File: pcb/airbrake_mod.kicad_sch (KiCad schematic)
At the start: 3 parts

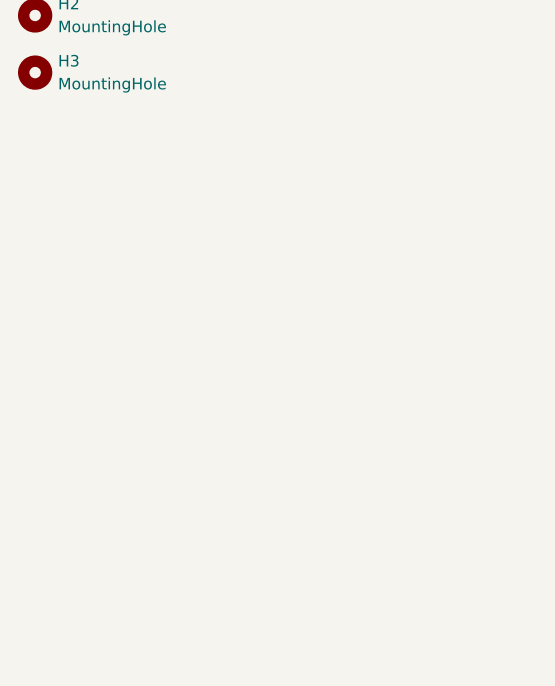
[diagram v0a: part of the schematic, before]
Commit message: Add USB
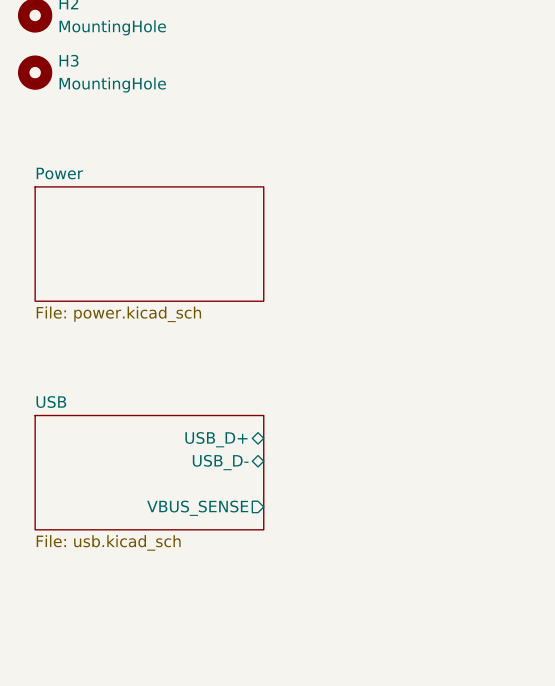
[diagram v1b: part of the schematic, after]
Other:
- added sheet Power (power.kicad_sch)
- added sheet USB (usb.kicad_sch)
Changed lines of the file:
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@@
+		)
+	)
+	(sheet
+		(at 25.4 50.8)
+		(size 25.4 12.7)
+		(exclude_from_sim no)
+		(in_bom yes)
+		(on_board yes)
+		(dnp no)
+		(fields_autoplaced yes)
+		(stroke
+			(width 0.1524)
+			(type solid)
+		)
+		(fill
+			(color 255 255 194 1.0000)
+		)
+		(property "Sheetname" "Power"
+			(at 25.4 50.0884 0)
+			(effects
+				(font
+					(size 1.27 1.27)
+				)
+				(justify left bottom)
+			)
+		)
+		(property "Sheetfile" "power.kicad_sch"
+			(at 25.4 64.0846 0)
+			(effects
+				(font
+					(size 1.27 1.27)
+				)
+				(justify left top)
+			)
+		)
+		(instances
+			(project "airbrake_mod"
+				(path "/1f4fd4ed-9886-4375-a5ac-dc32d5760936"
+					(page "3")
+				)
+			)
+		)
+	)
+	(sheet
+		(at 25.4 76.2)
+		(size 25.4 12.7)
+		(exclude_from_sim no)
+		(in_bom yes)
+		(on_board yes)
+		(dnp no)
+		(fields_autoplaced yes)
+		(stroke
+			(width 0.1524)
+			(type solid)
+		)
+		(fill
+			(color 255 255 194 1.0000)
+		)
+		(property "Sheetname" "USB"
+			(at 25.4 75.4884 0)
+			(effects
+				(font
+					(size 1.27 1.27)
+				)
+				(justify left bottom)
+			)
+		)
+		(property "Sheetfile" "usb.kicad_sch"
+			(at 25.4 89.4846 0)
+			(effects
+				(font
+					(size 1.27 1.27)
+				)
+				(justify left top)
+			)
+		)
+		(pin "USB_D+" bidirectional
+			(at 50.8 78.74 0)
+			(effects
+				(font
+					(size 1.27 1.27)
+				)
+				(justify right)
+			)
+		)
+		(pin "USB_D-" bidirectional
+			(at 50.8 81.28 0)
+			(effects
+				(font
+					(size 1.27 1.27)
+				)
+				(justify right)
+			)
+		)
+		(pin "VBUS_SENSE" output
+			(at 50.8 86.36 0)
+			(effects
+				(font
+					(size 1.27 1.27)
+				)
+				(justify right)
+			)
+		)
+		(instances
+			(project "airbrake_mod"
+				(path "/1f4fd4ed-9886-4375-a5ac-dc32d5760936"
+					(page "4")
+				)
+			)
 		)
 	)

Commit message: Begin power tree design
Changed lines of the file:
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@@
 	)
 	(sheet
-		(at 101.6 76.2)
+		(at 95.25 62.23)
 		(size 25.4 25.4)
 		(exclude_from_sim no)
@@
 		)
 		(property "Sheetname" "MCU"
-			(at 101.6 75.4884 0)
+			(at 95.25 61.5184 0)
 			(effects
 				(font
@@
 		)
 		(property "Sheetfile" "mcu.kicad_sch"
-			(at 101.6 102.1846 0)
+			(at 95.25 88.2146 0)
 			(effects
 				(font

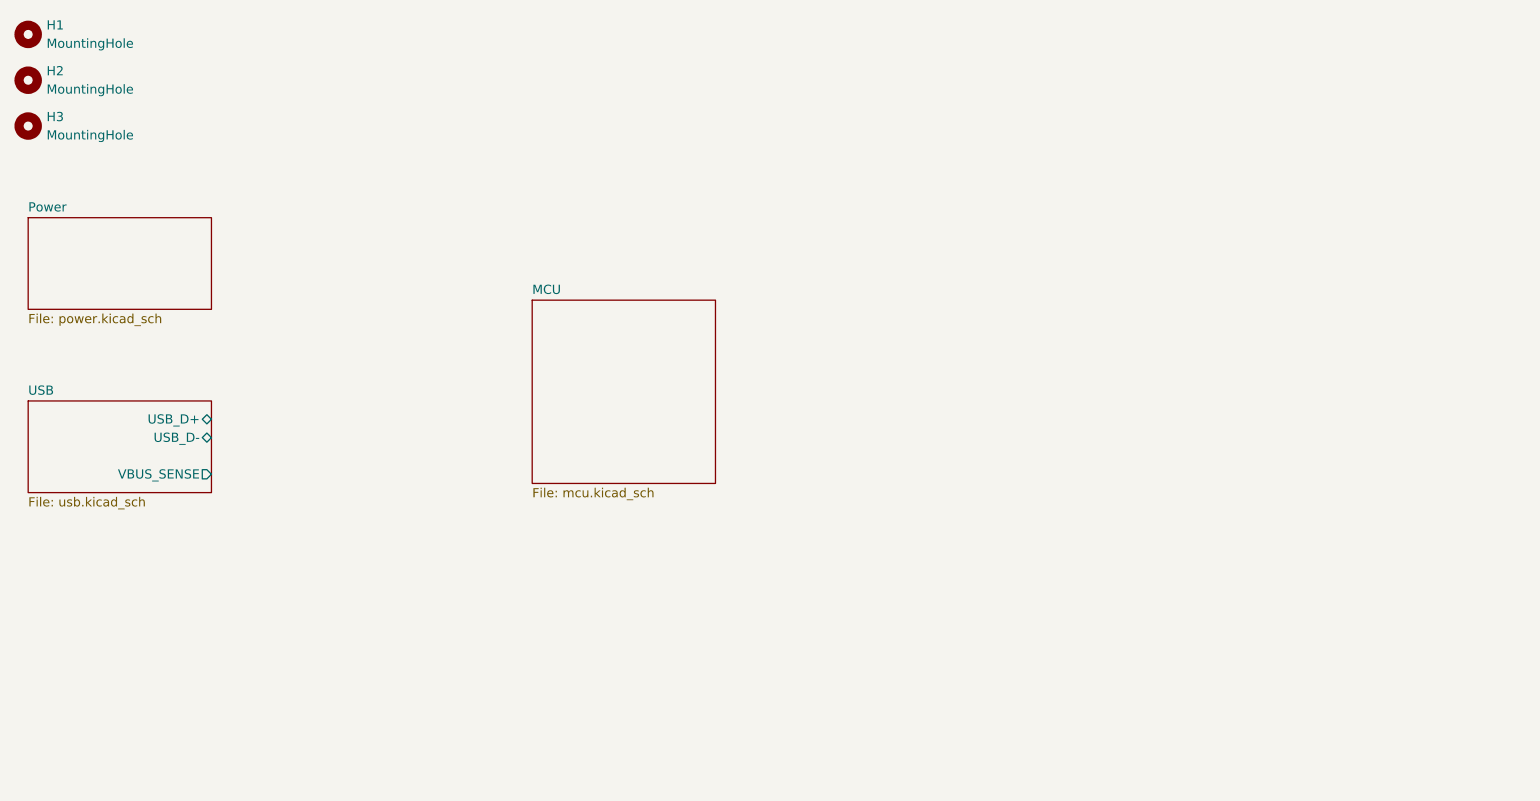
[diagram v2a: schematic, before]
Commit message: Implement flash memory connection
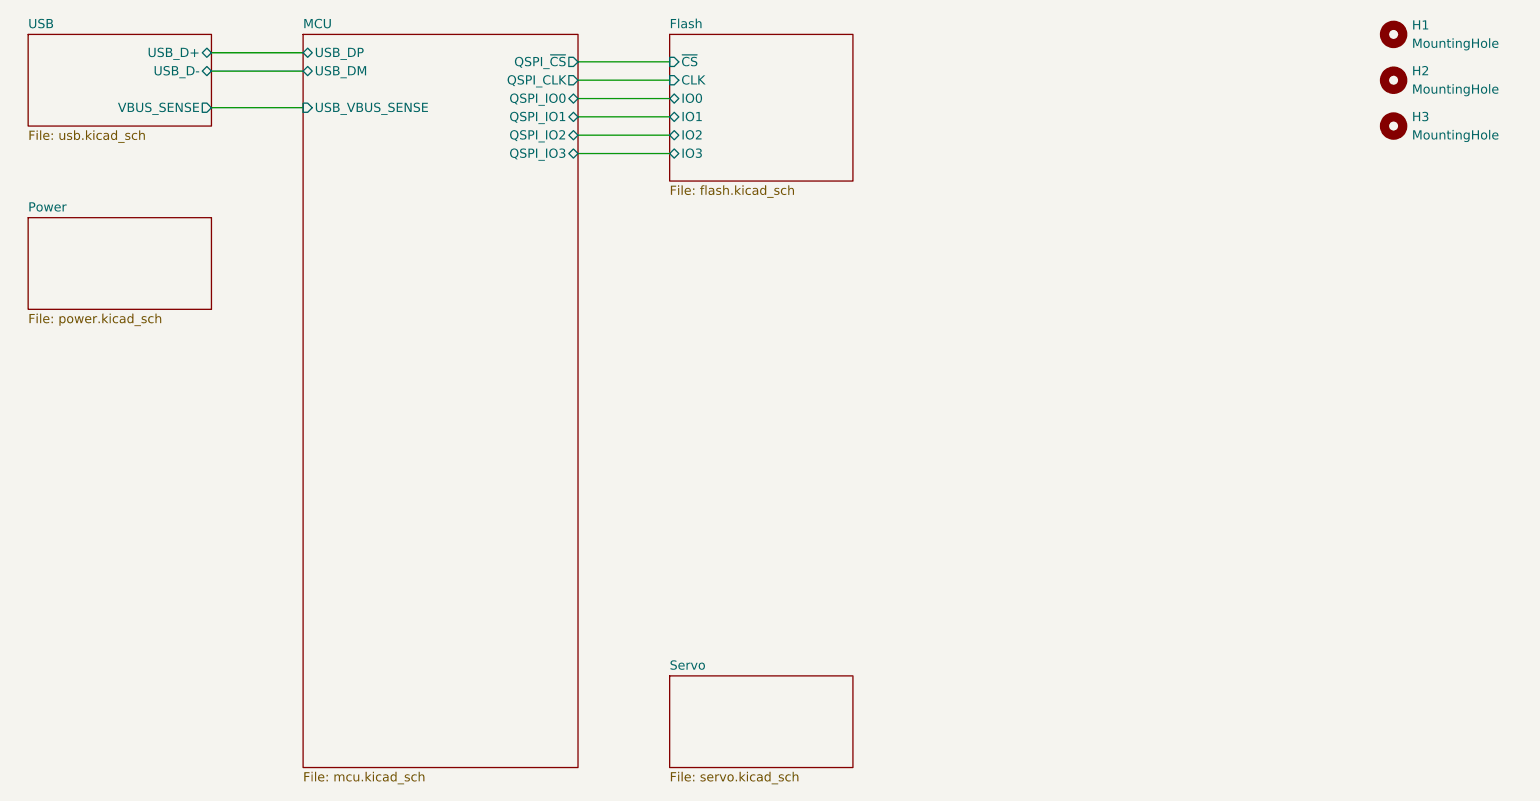
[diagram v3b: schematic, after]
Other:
- added sheet Flash (flash.kicad_sch)
- added sheet Servo (servo.kicad_sch)
- sheet MCU ports: added QSPI_CLK, QSPI_IO0, QSPI_IO1, QSPI_IO2, QSPI_IO3, QSPI_~{CS}, USB_DM, USB_DP, USB_VBUS_SENSE; removed none
- moved on the sheet: H1, H2, H3

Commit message: Add servo supporting info
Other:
- sheet Servo ports: added EN, PWM; removed none
- note added: "requires pin with TIM peripheral requires GPIO output"
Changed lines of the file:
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@@
 	(generator_version "9.0")
 	(paper "A4")
+	(text "requires pin with TIM peripheral\nrequires GPIO output"
+		(exclude_from_sim no)
+		(at 159.766 120.396 0)
+		(effects
+			(font
+				(size 1.27 1.27)
+			)
+		)
+	)
 	(wire
 		(pts
@@
 			)
 		)
+		(pin "EN" input
+			(at 114.3 119.38 180)
+			(effects
+				(font
+					(size 1.27 1.27)
+				)
+				(justify left)
+			)
+		)
+		(pin "PWM" input
+			(at 114.3 116.84 180)
+			(effects
+				(font
+					(size 1.27 1.27)
+				)
+				(justify left)
+			)
+		)

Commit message: Update project
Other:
- added sheet User Interface (user_interface.kicad_sch)
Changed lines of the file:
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@@
+	)
+	(sheet
+		(at 25.4 114.3)
+		(size 25.4 12.7)
+		(exclude_from_sim no)
+		(in_bom yes)
+		(on_board yes)
+		(dnp no)
+		(fields_autoplaced yes)
+		(stroke
+			(width 0.1524)
+			(type solid)
+		)
+		(fill
+			(color 255 255 194 1.0000)
+		)
+		(property "Sheetname" "User Interface"
+			(at 25.4 113.5884 0)
+			(effects
+				(font
+					(size 1.27 1.27)
+				)
+				(justify left bottom)
+			)
+		)
+		(property "Sheetfile" "user_interface.kicad_sch"
+			(at 25.4 127.5846 0)
+			(effects
+				(font
+					(size 1.27 1.27)
+				)
+				(justify left top)
+			)
+		)
+		(instances
+			(project "airbrake_mod"
+				(path "/1f4fd4ed-9886-4375-a5ac-dc32d5760936"
+					(page "7")
+				)
+			)
+		)
 	)
 	(sheet

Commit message: Add sensors sheet
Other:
- added sheet Debug (debug.kicad_sch)
- added sheet Sensors (sensors.kicad_sch)
- sheet MCU ports: added DEBUG_JTCK-SWCLK, DEBUG_JTDI, DEBUG_JTDO-SWO, DEBUG_JTMS-SWDIO, NRST, SERVO_EN, SERVO_SIG, VCP_RX, VCP_TX; removed none
- sheet User Interface ports: added LED0_B, LED0_G, LED0_R; removed none
